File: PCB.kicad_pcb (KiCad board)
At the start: 2 copper layers, 70 x 70 mm, 90 parts, among them J1 USB_C_Receptacle_USB2.0_16P, J10 Conn_01x02_Pin, J11 Conn_01x05_Pin, J13 Conn_01x04_Pin, J14 Conn_01x04_Pin, J15 Conn_01x02_Pin, J16 Conn_01x05_Pin, J17 Conn_01x03_Pin, J18 Conn_01x03_Pin, J19 Conn_01x03_Pin, J2 Conn_01x11_Socket, J20 Conn_01x03_Pin, J21 Conn_01x05_Pin, J22 Conn_01x04_Pin, J23 Conn_01x03_Pin, J24 Conn_01x03_Pin, J25 Conn_01x03_Pin, J26 Conn_01x03_Pin, J27 Conn_01x02_Pin, J3 Conn_01x08_Socket, J4 Conn_01x11_Socket, J5 Conn_01x02_Pin, J6 Conn_01x02_Pin, J7 Conn_01x02_Pin, J8 Conn_01x03_Pin, J9 Conn_01x02_Pin, SW1 SW_Push, SW2 SW_Push, U1 TB6612FNG, U10 MCP23008-xSO, U2 LTC4412xS6, U3 LTC4412xS6, U4 AMS1117-3.3 (UMW), U5 TB6612FNG, U6 ESP32-S3-WROOM-1, U7 TMC2209_SILENTSTEPSTICK, U8 TMC2209_SILENTSTEPSTICK, U9 TMC2209_SILENTSTEPSTICK

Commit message: changement driver + debut root pcb
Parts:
- removed C1: 100nF, Capacitor_SMD:C_0805_2012Metric_Pad1.18x1.45mm_HandSolder
- removed C14, C15: 100uF, Capacitor_SMD:CP_Elec_4x5.7
- removed JP1, JP2, JP3, JP4, JP5, JP6: Jumper_2_Open, Jumper:SolderJumper-2_P1.3mm_Open_RoundedPad1.0x1.5mm
- added C18: 100nF, Capacitor_SMD:C_0805_2012Metric_Pad1.18x1.45mm_HandSolder, B.Cu at (64.6, 90.0)
- added C19: 100nF, Capacitor_SMD:C_0805_2012Metric_Pad1.18x1.45mm_HandSolder, B.Cu at (43.6, 79.0)
- added C20: 100nF, Capacitor_SMD:C_0805_2012Metric_Pad1.18x1.45mm_HandSolder, B.Cu at (43.8, 90.2)
- added C4: 100u, Capacitor_THT:C_Radial_D8.0mm_H11.5mm_P3.50mm, F.Cu at (62.8, 74.0)
- added C6: 100u, Capacitor_THT:C_Radial_D8.0mm_H11.5mm_P3.50mm, F.Cu at (42.2, 74.0)
- added J12: Conn_01x02_Pin, Connector_PinHeader_2.54mm:PinHeader_1x02_P2.54mm_Vertical, F.Cu at (53.8, 89.7)
- added UART2: Conn_01x04_Pin, Connector_PinHeader_2.54mm:PinHeader_1x04_P2.54mm_Vertical, F.Cu at (64.8, 60.4)
- C11, C8: value 100nF -> 470u; footprint Capacitor_SMD:C_0805_2012Metric_Pad1.18x1.45mm_HandSolder -> Capacitor_THT:C_Radial_D8.0mm_H11.5mm_P3.50mm; moved to F.Cu
- C16: value 100uF -> 100nF; footprint Capacitor_SMD:CP_Elec_4x5.7 -> Capacitor_SMD:C_0805_2012Metric_Pad1.18x1.45mm_HandSolder; moved to B.Cu
- C17, J17, J18: moved to B.Cu
- C3: value 100nF -> 100u; footprint Capacitor_SMD:C_0805_2012Metric_Pad1.18x1.45mm_HandSolder -> Capacitor_THT:C_Radial_D8.0mm_H11.5mm_P3.50mm; moved to F.Cu
- R14: value 220k -> 180k
- R15: value 30k -> 33k
- U1, U5: value TB6612FNG -> ~; footprint Package_SO:SSOP-24_5.3x8.2mm_P0.65mm -> Package_SO:SOIC-8_3.9x4.9mm_P1.27mm
- moved C8 47.0 mm to (52.6, 106.2), turned to -90 degrees
- moved C3 37.7 mm to (98.0, 94.2), turned to -90 degrees
- moved C11 30.3 mm to (35.2, 62.6)
- moved U1 28.6 mm to (64.6, 84.4), turned to -90 degrees
- moved C16 23.5 mm to (64.6, 78.6)
- moved U5 20.5 mm to (43.7, 84.6), turned to -90 degrees
- moved J27 17.7 mm to (33.8, 89.5), turned to 0 degrees
- moved J9 13.8 mm to (36.4, 96.2), turned to -90 degrees
- moved R15 12.1 mm to (46.0, 95.6), turned to 90 degrees
- moved J18 10.4 mm to (45.2, 60.6)
- moved J17 10.4 mm to (45.2, 55.6)
- moved C17 10.3 mm to (45.2, 65.2), turned to -90 degrees
- moved R14 9.93 mm to (43.6, 95.6), turned to -90 degrees
- moved C13 9.05 mm to (41.2, 95.6), turned to -90 degrees
- moved R13 6.30 mm to (40.8, 108.0), turned to 90 degrees
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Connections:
- net GPIO1_D0_d renamed UART3_TX
- net GPIO1_D1_d renamed UART3_RX
- C11 pad 1: VCC_12V -> VCC_5V_GLOBAL
- C3 pad 1: 3V3 -> VCC_12V
- C8 pad 1: 3V3 -> VCC_12V
- J13 pad 1: M1- -> MOTORA1
- J13 pad 2: M2- -> MOTORA2
- J13 pad 3: M2+ -> MOTORA3
- J13 pad 4: M1+ -> MOTORA4
- J14 pad 1: M3- -> MOTORB1
- J14 pad 2: M4- -> MOTORB2
- J14 pad 3: M4+ -> MOTORB3
- J14 pad 4: M3+ -> MOTORB4
- J27 pad 1: VCC_5V_GLOBAL -> M2+
- J27 pad 2: VCC_12V -> M2-
- U1 pad 1: M1+ -> M1_IN2
- U1 pad 2: M1+ -> M1_IN1
- U1 pad 4: GND -> VCC_12V
- U1 pad 5: M1- -> M1+
- U1 pad 6: M1- -> M1+
- U1 pad 7: M2- -> M1-
- U1 pad 8: M2- -> M1-
- U5 pad 1: M3+ -> M2_IN2
- U5 pad 2: M3+ -> M2_IN1
- U5 pad 4: GND -> VCC_12V
- U5 pad 5: M3- -> M2+
- U5 pad 6: M3- -> M2+
- U5 pad 7: M4- -> M2-
- U5 pad 8: M4- -> M2-
- U6 pad 10: UART1+ -> UART1_TX+
- U6 pad 11: UART1- -> UART1_RX-
- U6 pad 12: M4_IN2 -> DIR2
- U6 pad 17: M1_IN1 -> STEP3
- U6 pad 18: M1_IN2 -> DIR3
- U6 pad 19: M2_IN1 -> M1_IN1
- U6 pad 20: M2_IN2 -> M1_IN2
- U6 pad 21: M1_PWM -> M2_IN1
- U6 pad 22: M2_PWM -> M2_IN2
- U6 pad 36: UART0- -> UART0_RX-
- U6 pad 37: UART0+ -> UART0_TX+
- U6 pad 5: M3_PWM -> STEP1
- U6 pad 6: M4_PWM -> DIR1
- U6 pad 7: M3_IN1 -> STEP2
- U6 pad 8: M3_IN2 -> MS1
- U6 pad 9: M4_IN1 -> MS2
- U7 pad 10: M1_IN1 -> STEP1
- U7 pad 14: Net-(JP2-B) -> MS2
- U7 pad 15: Net-(JP1-B) -> MS1
- U7 pad 3: M1- -> MOTORA1
- U7 pad 4: M2- -> MOTORA2
- U7 pad 5: M2+ -> MOTORA3
- U7 pad 6: M1+ -> MOTORA4
- U7 pad 9: M1_IN2 -> DIR1
- U8 pad 10: M3_IN1 -> STEP2
- U8 pad 14: Net-(JP4-B) -> MS2
- U8 pad 15: Net-(JP3-B) -> MS1
- U8 pad 3: M3- -> MOTORB1
- U8 pad 4: M4- -> MOTORB2
- U8 pad 5: M4+ -> MOTORB3
- U8 pad 6: M3+ -> MOTORB4
- U8 pad 9: M3_IN2 -> DIR2
- U9 pad 10: unconnected-(U9-STEP-Pad10) -> STEP3
- U9 pad 14: Net-(JP6-B) -> MS2
- U9 pad 15: Net-(JP5-B) -> MS1
- U9 pad 16: GND -> EN2
- U9 pad 9: unconnected-(U9-DIR-Pad9) -> DIR3
- UART1 pad 2: UART1- -> UART1_TX+
- UART1 pad 3: UART1+ -> UART1_RX-
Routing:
- net VCC_12V: track 0.00 -> 149.1 mm
- net VCC_5V_GLOBAL: track 0.00 -> 84.8 mm
- net VCC_12V_IN: track 0.00 -> 6.50 mm
- net MOTORC4: track 3.79 -> 0.13 mm
- net MOTORC3: track 3.79 -> 0.13 mm
- net MOTORC2: track 3.79 -> 0.13 mm
- net MOTORC1: track 3.79 -> 0.13 mm
- added copper zone on F.Cu, net VCC_12V
- added copper zone on F.Cu, net VCC_12V_IN
- added copper zone on F.Cu, net VCC_5V_BUCK
- added copper zone on F.Cu, net VCC_5V_USB
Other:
- board size 70 x 70 mm -> 143.4 x 71.9 mm
- board text added: "BUCK CONVERTER 12V to 5V"

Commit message: suite routage
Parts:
- moved VL1 45.2 mm to (98.8, 75.5), turned to -90 degrees
- moved J24 41.4 mm to (88.2, 75.5), turned to 90 degrees
- moved C3 40.1 mm to (58.5, 101.2)
- moved J3 40.1 mm to (73.9, 73.3), turned to 0 degrees
- moved J25 36.9 mm to (91.0, 75.5), turned to 90 degrees
- moved VL2 36.7 mm to (96.0, 75.5), turned to -90 degrees
- moved J11 35.3 mm to (92.3, 89.9), turned to 0 degrees
- moved VL0 33.8 mm to (89.8, 89.9), turned to 0 degrees
- moved U7 24.7 mm to (67.0, 103.2)
- moved J21 20.6 mm to (98.8, 89.7), turned to 0 degrees
- moved J13 18.5 mm to (79.5, 99.2), turned to 0 degrees
- moved AS2 18.4 mm to (92.1, 108.5), turned to -90 degrees
- moved J16 17.4 mm to (96.2, 89.7), turned to 0 degrees
- moved MPU1 16.2 mm to (85.8, 92.4), turned to 0 degrees
- moved AS1 15.4 mm to (92.1, 106.0), turned to -90 degrees
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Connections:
- J11 pad 5: VCC_5V -> VCC_5V_GLOBAL
- J16 pad 5: VCC_5V -> VCC_5V_GLOBAL
- J21 pad 5: VCC_5V -> VCC_5V_GLOBAL
- U10 pad 10: TEAM_BTN -> EN2
- U10 pad 11: LAUNCHPULL -> TEAM_BTN
- U10 pad 12: XSHUT0 -> LAUNCHPULL
- U10 pad 13: XSHUT1 -> EN1
- U10 pad 14: XSHUT2 -> XSHUT0
- U10 pad 15: XSHUT3 -> XSHUT1
- U10 pad 16: EN1 -> XSHUT2
- U10 pad 17: EN2 -> XSHUT3
- U6 pad 34: SDA2 -> SDA1
- U6 pad 35: SCL2 -> SDA2
- U6 pad 38: SCL1 -> SCL2
- U6 pad 39: SDA1 -> SCL1
- VL0 pad 5: VCC_5V -> VCC_5V_GLOBAL
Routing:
- net 3V3: track 0.00 -> 85.0 mm, vias 0 -> 3
- net VCC_12V: track 149.1 -> 104.4 mm
- net VCC_5V_GLOBAL: track 84.8 -> 119.7 mm
- net BOOT: track 0.00 -> 28.6 mm, vias 0 -> 1
- net XSHUT3: track 0.00 -> 25.0 mm
- net BLK: track 0.00 -> 24.1 mm
- net XSHUT2: track 0.00 -> 23.7 mm
- net XSHUT1: track 0.00 -> 22.6 mm
- net CS: track 0.00 -> 21.0 mm
- net XSHUT0: track 0.00 -> 20.7 mm
- net MOTORA4: track 0.00 -> 20.5 mm
- net EN1: track 0.00 -> 20.3 mm
- net BAU+: track 0.00 -> 19.6 mm, vias 0 -> 1
- net LAUNCHPULL: track 0.00 -> 17.1 mm
- net DC: track 0.00 -> 16.9 mm
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
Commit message: routage
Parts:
- removed AO4407A3: PMOS, Package_SO:SOIC-8-1EP_3.9x4.9mm_P1.27mm_EP2.29x3mm_ThermalVias
- removed J25, VL2: Conn_01x03_Pin, Jumper:SolderJumper-3_P1.3mm_Open_Pad1.0x1.5mm
- removed R16: 10k, Resistor_SMD:R_1206_3216Metric_Pad1.30x1.75mm_HandSolder
- moved J12 25.4 mm to (79.5, 92.4)
- moved J19 23.5 mm to (97.2, 77.2), turned to 180 degrees
- moved J20 20.0 mm to (87.3, 77.2), turned to 0 degrees
- moved J27 12.5 mm to (45.2, 94.6), turned to -90 degrees
- moved C13 10.9 mm to (52.1, 95.6)
- moved R15 8.60 mm to (54.6, 95.5)
- moved AS1 7.60 mm to (84.5, 105.9), turned to 90 degrees
- moved AS2 7.60 mm to (84.5, 108.4), turned to 90 degrees
- moved R14 6.00 mm to (49.6, 95.6)
- moved J9 3.74 mm to (33.9, 93.4), turned to 0 degrees
- moved U2 3.55 mm to (73.4, 46.0)
- moved R5 2.75 mm to (96.0, 70.8)
- moved R7 2.30 mm to (98.3, 70.7)
- moved J8 2.00 mm to (79.0, 48.6)
- moved VL1 1.77 mm to (97.3, 74.5), turned to 180 degrees
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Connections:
- net UART3_RX renamed UART3_RX-
- net UART3_TX renamed UART3_TX+
- J16 pad 2: Net-(J16-Pin_2) -> Net-(J11-Pin_2)
- J16 pad 3: Net-(J16-Pin_3) -> Net-(J11-Pin_3)
- J21 pad 2: Net-(J16-Pin_2) -> Net-(J11-Pin_2)
- J21 pad 3: Net-(J16-Pin_3) -> Net-(J11-Pin_3)
- U10 pad 10: EN2 -> EN1
- U10 pad 13: EN1 -> EN2
- U6 pad 10: UART1_TX+ -> DIR3
- U6 pad 12: DIR2 -> UART1_TX+
- U6 pad 17: STEP3 -> SERVO0
- U6 pad 18: DIR3 -> SERVO1
- U6 pad 19: M1_IN1 -> M2_IN1
- U6 pad 20: M1_IN2 -> M2_IN2
- U6 pad 21: M2_IN1 -> M1_IN1
- U6 pad 22: M2_IN2 -> M1_IN2
- U6 pad 23: VCC_CALC -> MS1
- U6 pad 24: SERVO0 -> MS2
- U6 pad 25: SERVO1 -> VCC_CALC
- U6 pad 38: SCL2 -> SCL1
- U6 pad 39: SCL1 -> SCL2
- U6 pad 8: MS1 -> DIR2
- U6 pad 9: MS2 -> STEP3
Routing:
- net VCC_5V_GLOBAL: track 119.7 -> 200.0 mm, vias 0 -> 1
- net STEP1: track 0.00 -> 61.4 mm, vias 0 -> 1
- net EN2: track 0.00 -> 57.3 mm, vias 0 -> 2
- net DIR1: track 0.00 -> 56.7 mm, vias 0 -> 1
- net MS2: track 0.00 -> 52.8 mm
- net XSHUT3: track 25.0 -> 75.1 mm, vias 0 -> 4
- net MS1: track 0.00 -> 49.9 mm
- net XSHUT2: track 23.7 -> 72.1 mm, vias 0 -> 4
- net XSHUT1: track 22.6 -> 69.0 mm, vias 0 -> 4
- net XSHUT0: track 20.7 -> 66.4 mm, vias 0 -> 4
- net STEP3: track 0.00 -> 43.8 mm, vias 0 -> 1
- net DIR3: track 0.00 -> 41.5 mm, vias 0 -> 1
- net VCC_CALC: track 0.00 -> 33.2 mm, vias 0 -> 1
- net Net-(J11-Pin_3): track 1.21 -> 33.3 mm, vias 1 -> 2
- net EN1: track 20.3 -> 51.5 mm, vias 0 -> 1
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- added copper zone on F.Cu, net 3V3
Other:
- board size 143.4 x 71.9 mm -> 152 x 70 mm

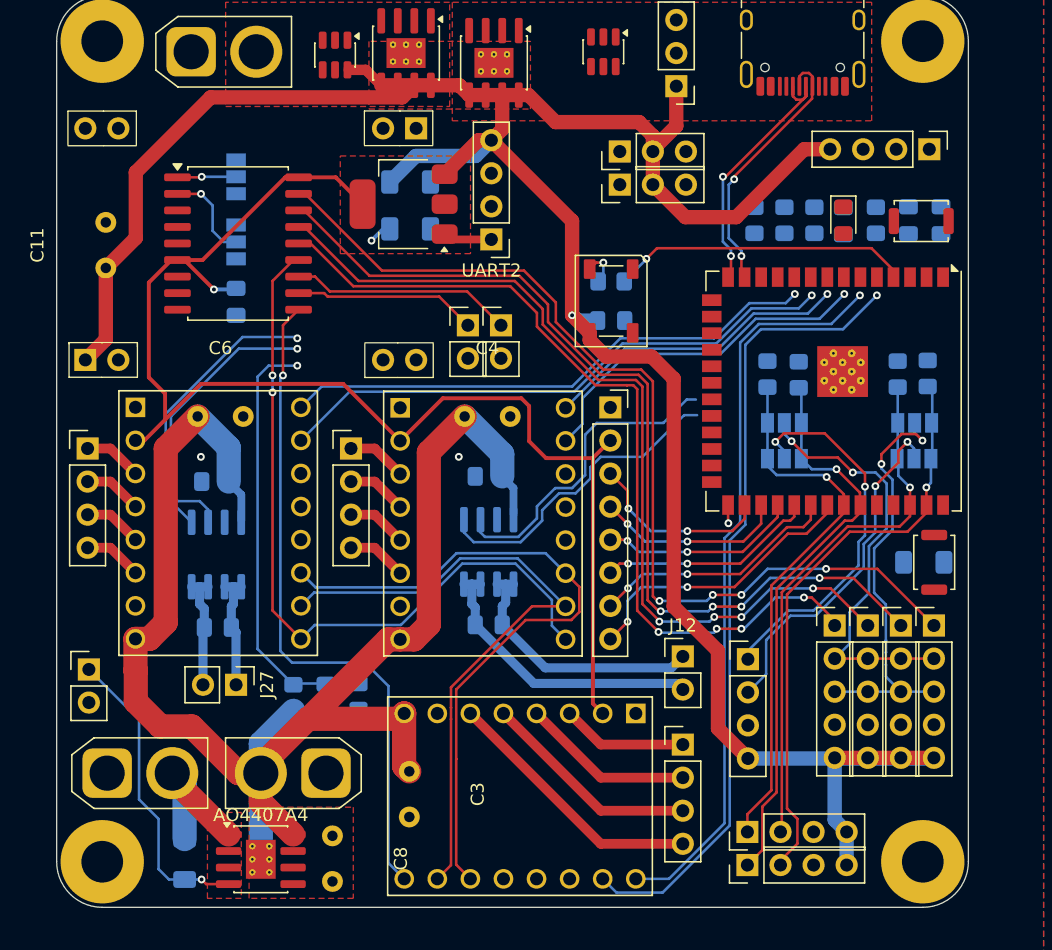
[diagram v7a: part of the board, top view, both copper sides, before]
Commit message: suite routage + séparation 2eme pcb avec 2 nema
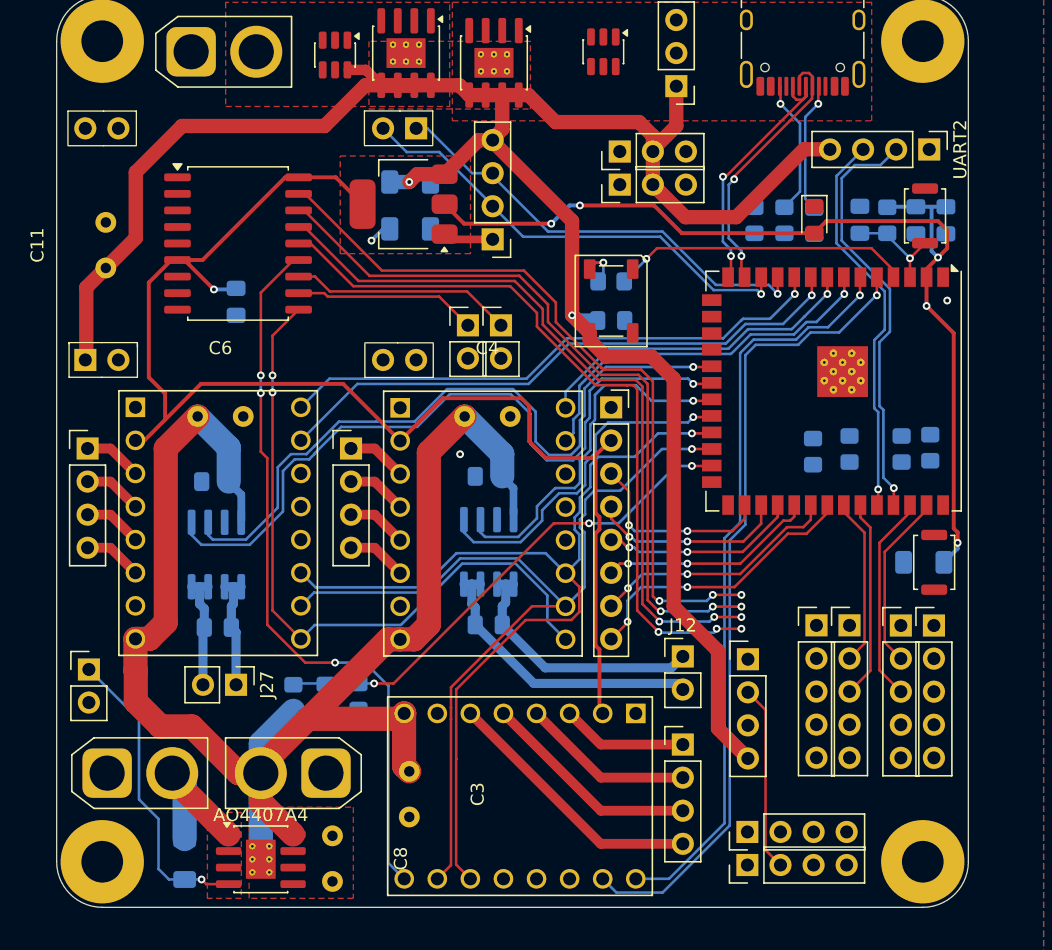
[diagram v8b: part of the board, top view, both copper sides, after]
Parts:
- removed J17, J18, J19, J20, J24, VL1: Conn_01x03_Pin, Jumper:SolderJumper-3_P1.3mm_Open_Pad1.0x1.5mm
- moved UART2 34.3 mm to (98.4, 53.5), turned to -90 degrees
- moved UART1 34.2 mm to (64.9, 60.4), turned to 180 degrees
- moved R6 13.7 mm to (98.5, 76.4)
- moved R7 8.35 mm to (92.3, 76.5)
- moved R8 6.00 mm to (89.5, 76.7)
- moved R5 5.76 mm to (96.3, 76.5)
- moved R3 2.30 mm to (89.6, 59.0)
- moved R2 2.30 mm to (87.3, 58.9), turned to -90 degrees
- moved D1 2.23 mm to (89.6, 58.9)
- moved J11 1.40 mm to (92.3, 90.0)
- moved VL0 1.40 mm to (89.8, 90.0)
- moved C2 1.28 mm to (93.1, 58.9), turned to 90 degrees
- moved R1 0.88 mm to (95.2, 58.9), turned to -90 degrees
- moved C10 0.58 mm to (97.4, 58.9)
- moved SW2 0.50 mm to (98.1, 58.6), turned to -90 degrees
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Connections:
- AS1 pad 1: SDA1 -> GND
- AS1 pad 3: GND -> SDA1
- AS2 pad 1: SDA2 -> GND
- AS2 pad 3: GND -> SDA2
- J11 pad 2: Net-(J11-Pin_2) -> SDA2
- J11 pad 3: Net-(J11-Pin_3) -> SCL2
- J16 pad 2: Net-(J11-Pin_2) -> SDA1
- J16 pad 3: Net-(J11-Pin_3) -> SCL1
- J2 pad 1: UART3_TX+ -> UART1_RX-
- J2 pad 2: UART3_RX- -> UART1_TX+
- J21 pad 2: Net-(J11-Pin_2) -> SDA1
- J21 pad 3: Net-(J11-Pin_3) -> SCL1
- MPU1 pad 1: Net-(J20-Pin_2) -> SDA2
- MPU1 pad 2: Net-(J19-Pin_2) -> SCL2
- U10 pad 1: Net-(J17-Pin_2) -> SCL1
- U10 pad 2: Net-(J18-Pin_2) -> SDA1
- U6 pad 23: MS1 -> MS2
- U6 pad 24: MS2 -> MS1
- U6 pad 34: SDA1 -> SDA2
- U6 pad 35: SDA2 -> SCL2
- U6 pad 39: SCL2 -> SDA1
- U7 pad 16: EN1 -> EN2
- U8 pad 16: EN2 -> EN1
- U9 pad 16: EN2 -> EN1
- VL0 pad 2: Net-(J11-Pin_2) -> SDA2
- VL0 pad 3: Net-(J11-Pin_3) -> SCL2
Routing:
- net 3V3: track 104.3 -> 182.3 mm, vias 2 -> 7
- net UART1_TX+: track 0.00 -> 35.6 mm, vias 0 -> 1
- net VCC_5V_GLOBAL: track 200.0 -> 164.8 mm, vias 1 -> 2
- net M2_IN2: track 21.7 -> 56.5 mm
- net UART1_RX-: track 0.00 -> 34.4 mm, vias 0 -> 1
- net Net-(J11-Pin_3): track 33.3 -> 0.00 mm, vias 2 -> 0
- net Net-(J11-Pin_2): track 33.0 -> 0.00 mm, vias 2 -> 0
- net M2_IN1: track 22.2 -> 55.0 mm
- net UART0_TX+: track 0.00 -> 32.8 mm, vias 0 -> 1
- net SDA2: track 43.6 -> 12.9 mm, vias 1 -> 0
- net UART0_RX-: track 0.00 -> 30.2 mm, vias 0 -> 1
- net Net-(J20-Pin_2): track 29.1 -> 0.00 mm, vias 2 -> 0
- net SDA1: track 41.8 -> 13.6 mm, vias 1 -> 0
- net Net-(J19-Pin_2): track 26.9 -> 0.00 mm, vias 2 -> 0
- net SCL1: track 41.0 -> 16.0 mm, vias 1 -> 0
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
